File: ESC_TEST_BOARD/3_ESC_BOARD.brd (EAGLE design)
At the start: 119.2 x 68.1 mm, 82 parts, among them J3 AVR_SPI_PROG_3X2NS, U2 ATMEGA328P_TQFP, U4 PCA9685

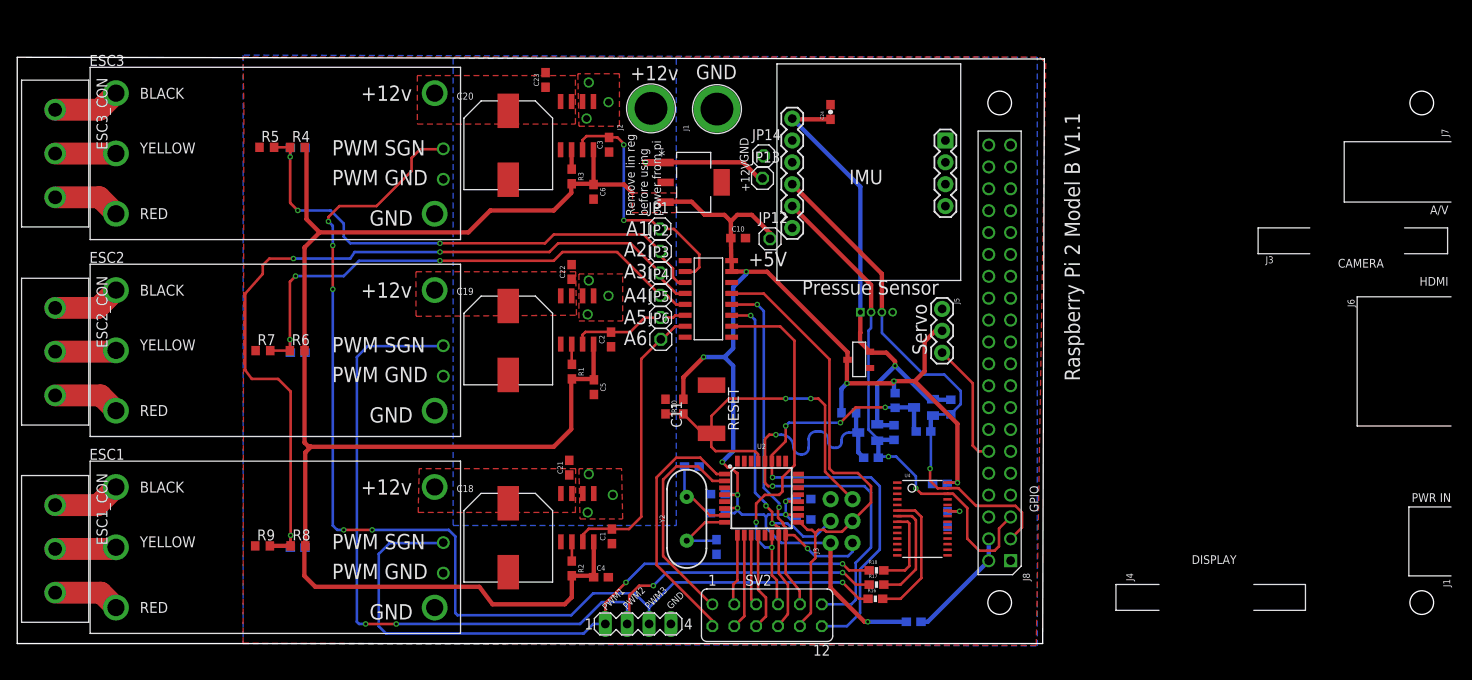
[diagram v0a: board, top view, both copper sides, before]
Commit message: Addressing comments made by Kyle and Carolyn
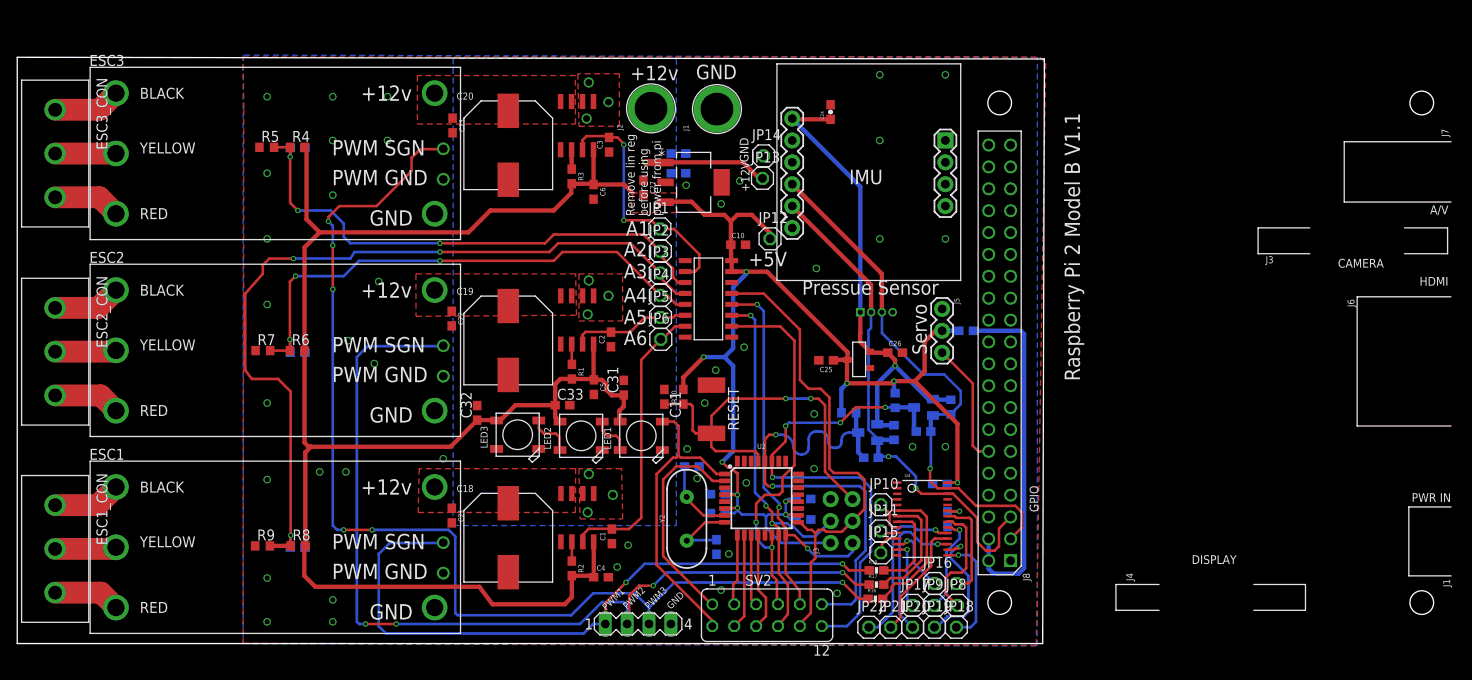
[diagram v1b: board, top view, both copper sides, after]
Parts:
- added C25, C26, C27, C29: 0.1uF, SparkFun-Capacitors:0603
- added C30: 10uF, SparkFun-Capacitors:0603
- added C31, C32, C33: (no value), rcl:C0603
- added JP10, JP11, JP15, JP16, JP17, JP18, JP19, JP20, JP21, JP22, JP7, JP8, JP9: (no value), pinhead:1X01
- added LED1, LED2, LED3: WS2812B5050, microbuilder:WS2812B
- moved R19 34.3 mm to (110.4, 36.3)
- moved C22 14.9 mm to (50.6, 37.7), turned to 270 degrees
- moved C21 14.7 mm to (50.6, 14.9), turned to 270 degrees
- moved C23 12.0 mm to (50.7, 60.2), turned to 270 degrees
- moved C11 1.15 mm to (75.3, 28.7)
- moved R10 1.14 mm to (77.5, 28.7)
- moved C10 0.76 mm to (83.9, 46.3)
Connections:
- new net OUT1: LED1.2-DOUT, LED2.4-DIN
- new net OUT2: LED2.2-DOUT, LED3.4-DIN
- new net OUT3: LED3.2-DOUT
- net +12V: now also C29.2, C30.2
- net +5V: now also C25.1, C27.2, C31.1, C32.1, C33.1, LED1.1-VDD, LED2.1-VDD, LED3.1-VDD
- net 3.3V: now also C26.1
- net GND: now also C25.2, C26.2, C27.1, C29.1, C30.1, C31.2, C32.2, C33.2, LED1.3-GND, LED2.3-GND, LED3.3-GND
- net PD3: now also LED1.4-DIN
- net PWM_CON_10: now also JP20.1
- net PWM_CON_11: now also JP21.1
- net PWM_CON_12: now also JP22.1
- net PWM_CON_13: now also JP9.1
- net PWM_CON_14: now also JP8.1
- net PWM_CON_15: now also JP7.1
- net PWM_CON_3: now also JP10.1
- net PWM_CON_4: now also JP11.1
- net PWM_CON_5: now also JP15.1
- net PWM_CON_6: now also JP16.1
- net PWM_CON_7: now also JP17.1
- net PWM_CON_8: now also JP18.1
- net PWM_CON_9: now also JP19.1
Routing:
- net VCC: track 13.3 -> 41.3 mm
- net PWM_CON_12: track 0.00 -> 19.6 mm, vias 0 -> 1
- net PWM_CON_10: track 0.00 -> 17.5 mm, vias 0 -> 1
- net PWM_CON_9: track 0.00 -> 15.5 mm, vias 0 -> 1
- net PWM_CON_14: track 0.00 -> 14.4 mm
- net PWM_CON_11: track 0.00 -> 13.9 mm
- net PWM_CON_8: track 0.00 -> 13.2 mm, vias 0 -> 1
- net PWM_CON_15: track 0.00 -> 11.9 mm
- net PWM_CON_13: track 0.00 -> 11.5 mm, vias 0 -> 1
- net PWM_CON_7: track 0.00 -> 7.89 mm, vias 0 -> 1
- net PWM_CON_6: track 0.00 -> 7.86 mm, vias 0 -> 1
- net PD3: track 29.6 -> 35.5 mm
- net OUT2: track 0.00 -> 5.27 mm
- net OUT1: track 0.00 -> 4.76 mm
- net +5V: track 345.0 -> 340.5 mm, vias 11 -> 10
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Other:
- board text added: "ESC Board Version1: 11/11/2017 Jacob Bobson Luke McBee Cynthia Zatlkowicz Jason King"
- board text removed: "ESC Board Version1: 11/11/2017 Jacob Bobson Luke McBee Cynthia Zatlkowicz Grant Geyer Josh Burdine Melchor De La Garza"

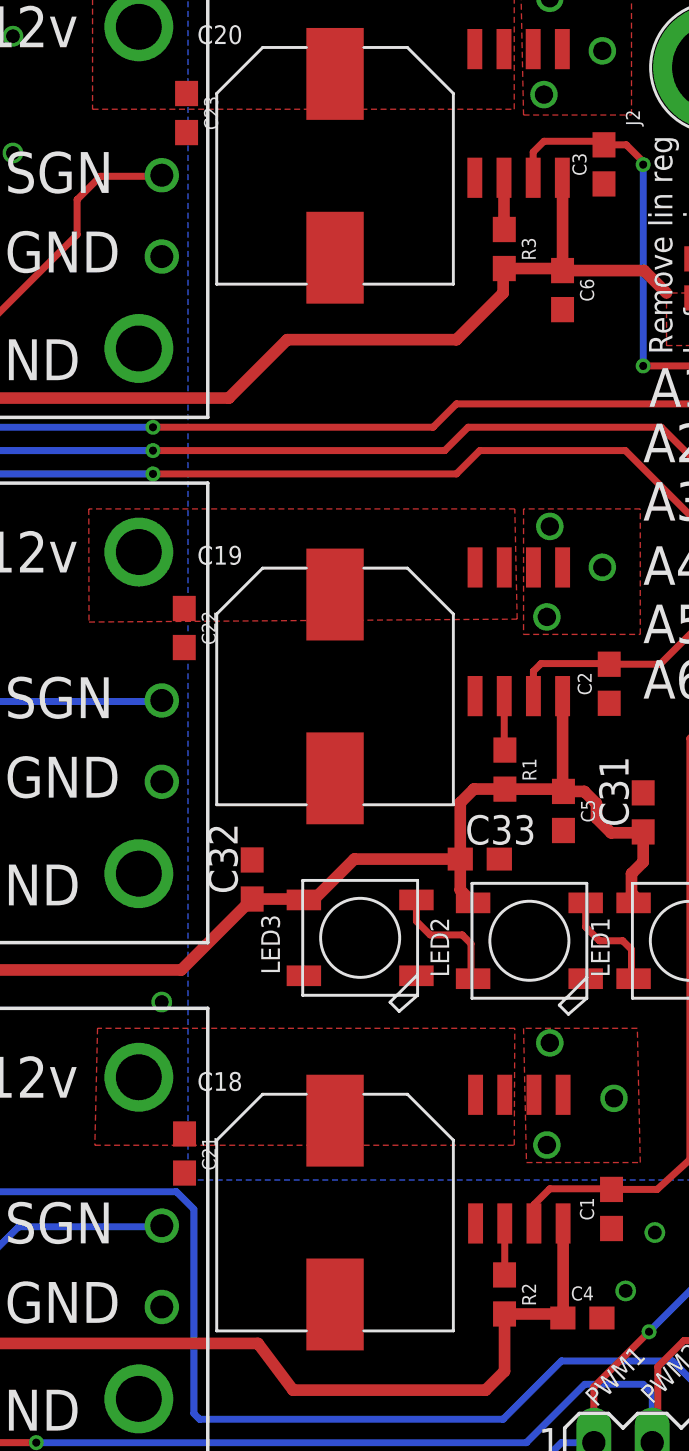
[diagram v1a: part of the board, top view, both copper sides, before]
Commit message: Added capacitor values to unmarked capacitors
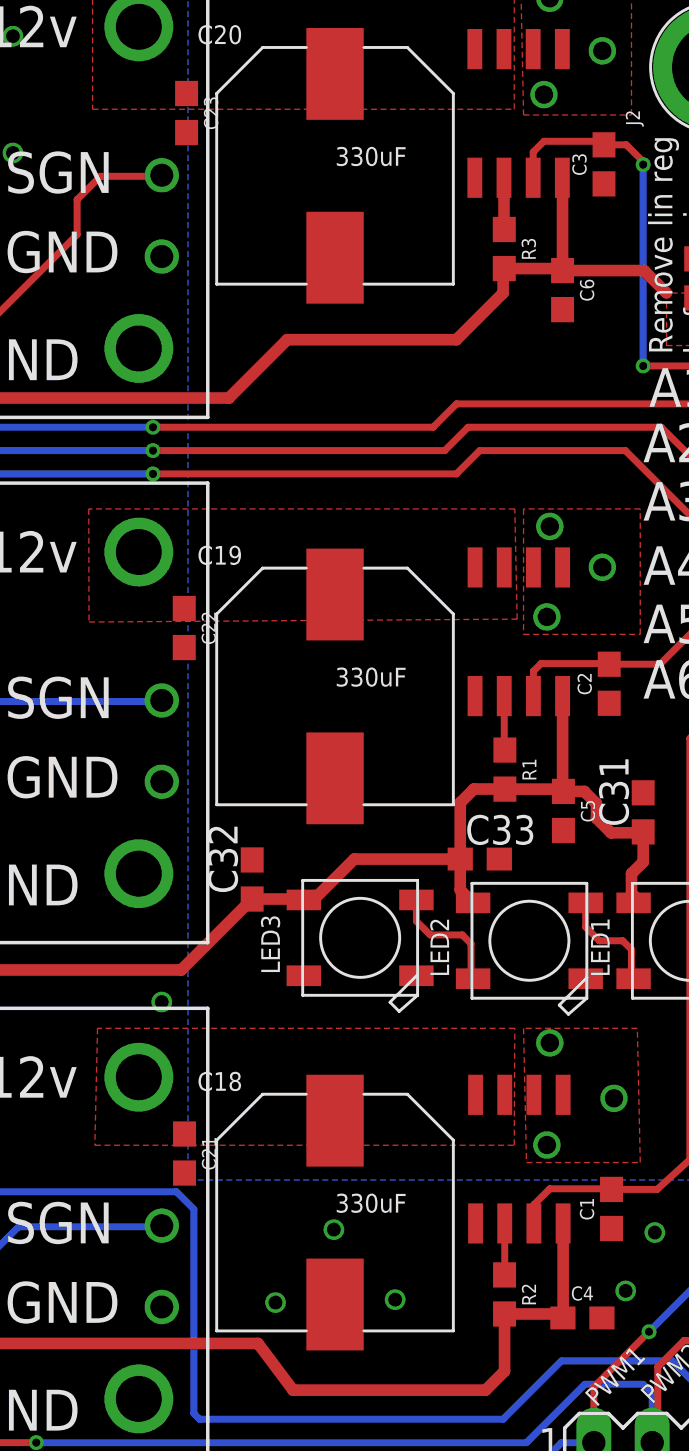
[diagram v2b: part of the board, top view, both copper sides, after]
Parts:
- C11, C12, C13, C14, C15, C31, C32, C33: value (none) -> 0.1uF
- C16, C17: value (none) -> 22pF
- C18, C19, C20: value (none) -> 330uF
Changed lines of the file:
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@@
 <setting verticaltext="up"/>
 </settings>
-<grid distance="5" unitdist="mil" unit="mil" style="lines" multiple="1" display="no" altdistance="1" altunitdist="mil" altunit="mil"/>
+<grid distance="0.1" unitdist="mm" unit="mm" style="lines" multiple="1" display="no" altdistance="1" altunitdist="mil" altunit="mil"/>
 <layers>
 <layer number="1" name="Top" color="4" fill="1" visible="yes" active="yes"/>
@@
 <element name="J3" library="SparkFun-Connectors" library_urn="urn:adsk.eagle:library:513" package="2X3-NS" package3d_urn="urn:adsk.eagle:package:38013/1" value="AVR_SPI_PROG_3X2NS" x="95.894" y="14.236" rot="R90"/>
 <element name="RESET" library="DiscreteComponents" package="SW_2512" value="" x="80.797" y="27.216" rot="R270"/>
-<element name="C11" library="rcl" library_urn="urn:adsk.eagle:library:334" package="C0603" package3d_urn="urn:adsk.eagle:package:23616/2" value="" x="75.3262" y="28.6682" rot="R270"/>
+<element name="C11" library="rcl" library_urn="urn:adsk.eagle:library:334" package="C0603" package3d_urn="urn:adsk.eagle:package:23616/2" value="0.1uF" x="75.3262" y="28.6682" rot="R270"/>
 <element name="R10" library="SparkFun-Resistors" library_urn="urn:adsk.eagle:library:532" package="0603" package3d_urn="urn:adsk.eagle:package:39650/1" value=" " x="77.529665625" y="28.6682" rot="R90">
 <attribute name="PROD_ID" value=" " x="53.829665625" y="-10.5318" size="1.778" layer="27" rot="R90" display="off"/>
 </element>
-<element name="C12" library="rcl" library_urn="urn:adsk.eagle:library:334" package="C0603" package3d_urn="urn:adsk.eagle:package:23616/2" value="" x="81.531" y="17.358" rot="MR0"/>
-<element name="C13" library="rcl" library_urn="urn:adsk.eagle:library:334" package="C0603" package3d_urn="urn:adsk.eagle:package:23616/2" value="" x="81.531" y="15.158" rot="MR0"/>
-<element name="C14" library="rcl" library_urn="urn:adsk.eagle:library:334" package="C0603" package3d_urn="urn:adsk.eagle:package:23616/2" value="" x="91.484" y="16.793" rot="MR180"/>
-<element name="C15" library="rcl" library_urn="urn:adsk.eagle:library:334" package="C0603" package3d_urn="urn:adsk.eagle:package:23616/2" value="" x="91.484" y="14.421" rot="MR180"/>
+<element name="C12" library="rcl" library_urn="urn:adsk.eagle:library:334" package="C0603" package3d_urn="urn:adsk.eagle:package:23616/2" value="0.1uF" x="81.531" y="17.358" rot="MR0"/>
+<element name="C13" library="rcl" library_urn="urn:adsk.eagle:library:334" package="C0603" package3d_urn="urn:adsk.eagle:package:23616/2" value="0.1uF" x="81.531" y="15.158" rot="MR0"/>
+<element name="C14" library="rcl" library_urn="urn:adsk.eagle:library:334" package="C0603" package3d_urn="urn:adsk.eagle:package:23616/2" value="0.1uF" x="91.484" y="16.793" rot="MR180"/>
+<element name="C15" library="rcl" library_urn="urn:adsk.eagle:library:334" package="C0603" package3d_urn="urn:adsk.eagle:package:23616/2" value="0.1uF" x="91.484" y="14.421" rot="MR180"/>
 <element name="Y2" library="SparkFun-Clocks" library_urn="urn:adsk.eagle:library:511" package="HC49US" package3d_urn="urn:adsk.eagle:package:37515/1" value="" x="77.922" y="14.498" rot="R90"/>
-<element name="C16" library="rcl" library_urn="urn:adsk.eagle:library:334" package="C0603" package3d_urn="urn:adsk.eagle:package:23616/2" value="" x="78.511" y="20.566" rot="MR180"/>
-<element name="C17" library="rcl" library_urn="urn:adsk.eagle:library:334" package="C0603" package3d_urn="urn:adsk.eagle:package:23616/2" value="" x="81.372" y="11.225" rot="MR270"/>
-<element name="C18" library="PowerComponents" package="CPOL-US(10.3_10.3MM)" value="" x="57.2" y="12.3"/>
-<element name="C19" library="PowerComponents" package="CPOL-US(10.3_10.3MM)" value="" x="57.2" y="35.2"/>
-<element name="C20" library="PowerComponents" package="CPOL-US(10.3_10.3MM)" value="" x="57.2" y="57.86"/>
+<element name="C16" library="rcl" library_urn="urn:adsk.eagle:library:334" package="C0603" package3d_urn="urn:adsk.eagle:package:23616/2" value="22pF" x="78.511" y="20.566" rot="MR180"/>
+<element name="C17" library="rcl" library_urn="urn:adsk.eagle:library:334" package="C0603" package3d_urn="urn:adsk.eagle:package:23616/2" value="22pF" x="81.372" y="11.225" rot="MR270"/>
+<element name="C18" library="PowerComponents" package="CPOL-US(10.3_10.3MM)" value="330uF" x="57.2" y="12.3"/>
+<element name="C19" library="PowerComponents" package="CPOL-US(10.3_10.3MM)" value="330uF" x="57.2" y="35.2"/>
+<element name="C20" library="PowerComponents" package="CPOL-US(10.3_10.3MM)" value="330uF" x="57.2" y="57.86"/>
 <element name="JP1" library="pinhead" library_urn="urn:adsk.eagle:library:325" package="1X01" package3d_urn="urn:adsk.eagle:package:22485/1" value="" x="74.803" y="48.145"/>
 <element name="JP2" library="pinhead" library_urn="urn:adsk.eagle:library:325" package="1X01" package3d_urn="urn:adsk.eagle:package:22485/1" value="" x="74.854" y="45.552"/>
@@
 </element>
 <element name="LED1" library="microbuilder" package="WS2812B" value="WS2812B5050" x="72.644" y="24.13" rot="R180"/>
-<element name="C31" library="rcl" library_urn="urn:adsk.eagle:library:334" package="C0603" package3d_urn="urn:adsk.eagle:package:23616/2" value="" x="70.612" y="29.718" rot="R90"/>
+<element name="C31" library="rcl" library_urn="urn:adsk.eagle:library:334" package="C0603" package3d_urn="urn:adsk.eagle:package:23616/2" value="0.1uF" x="70.612" y="29.718" rot="R90"/>
 <element name="LED2" library="microbuilder" package="WS2812B" value="WS2812B5050" x="65.659" y="24.13" rot="R180"/>
-<element name="C32" library="rcl" library_urn="urn:adsk.eagle:library:334" package="C0603" package3d_urn="urn:adsk.eagle:package:23616/2" value="" x="53.594" y="26.797" rot="R90"/>
+<element name="C32" library="rcl" library_urn="urn:adsk.eagle:library:334" package="C0603" package3d_urn="urn:adsk.eagle:package:23616/2" value="0.1uF" x="53.594" y="26.797" rot="R90"/>
 <element name="LED3" library="microbuilder" package="WS2812B" value="WS2812B5050" x="58.293" y="24.257" rot="R180"/>
-<element name="C33" library="rcl" library_urn="urn:adsk.eagle:library:334" package="C0603" package3d_urn="urn:adsk.eagle:package:23616/2" value="" x="63.5" y="27.686"/>
+<element name="C33" library="rcl" library_urn="urn:adsk.eagle:library:334" package="C0603" package3d_urn="urn:adsk.eagle:package:23616/2" value="0.1uF" x="63.5" y="27.686"/>
 </elements>
 <signals>
@@
 <contactref element="C32" pad="2"/>
 <contactref element="C33" pad="2"/>
+<via x="59.817" y="8.509" extent="1-16" drill="0.6"/>
+<via x="54.61" y="8.382" extent="1-16" drill="0.6"/>
+<via x="57.15" y="11.557" extent="1-16" drill="0.6"/>
 </signal>
 <signal name="+12V">
